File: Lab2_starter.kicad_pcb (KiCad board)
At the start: 4 copper layers, 139.7 x 101.6 mm, 77 parts, among them J1 973582101, J10 Conn_01x02, J11 Conn_01x02, J12 Conn_01x02, J13 Conn_01x02, J14 Conn_01x02, J15 Conn_01x02, J16 Conn_01x02, J2 973582100, J3 973582101, J4 973582100, J5 Conn_01x01, J6 Conn_01x01, J7 Conn_01x02, J8 Conn_01x02, J9 Conn_01x02, Q1 NMOS, Q2 NMOS, SW1 SW_Push_DPDT, U1 IR2010, U2 CT416-HSN820DR, U3 LAUNCHXL-F28P55X_BottomHalf

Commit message: Add Kicad files
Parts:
- C16: moved to B.Cu
- HS1, HS2: footprint ECE462L:HSS-B20-NPR-02 -> ECE462L:HSS-B20-NPS-01
- moved C16 241.9 mm to (50.7, 76.2), turned to -90 degrees
- moved C15 210.3 mm to (72.5, 82.0), turned to -90 degrees
- moved C12 206.2 mm to (76.9, 82.0), turned to -90 degrees
- moved Q1 205.8 mm to (77.5, 78.6)
- moved C9 203.8 mm to (74.7, 82.0), turned to -90 degrees
- moved Q2 197.6 mm to (86.0, 81.8), turned to 180 degrees
- moved HS2 186.2 mm to (80.4, 68.5)
- moved HS1 174.2 mm to (83.9, 92.0), turned to 180 degrees
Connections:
- C1 pad 2: Net-(U2-GND) -> GND
- C12 pad 1: unconnected-(C12-Pad1) -> Vout
- C12 pad 2: unconnected-(C12-Pad2) -> GND
- C15 pad 1: unconnected-(C15-Pad1) -> Vout
- C15 pad 2: unconnected-(C15-Pad2) -> GND
- C16 pad 1: unconnected-(C16-Pad1) -> Vout
- C16 pad 2: unconnected-(C16-Pad2) -> GND
- C3 pad 1: unconnected-(C3-Pad1) -> Vboot
- C3 pad 2: unconnected-(C3-Pad2) -> Vsw
- C4 pad 1: unconnected-(C4-Pad1) -> +12V
- C4 pad 2: unconnected-(C4-Pad2) -> GND
- C6 pad 1: unconnected-(C6-Pad1) -> Vin
- C6 pad 2: unconnected-(C6-Pad2) -> GND
- C9 pad 1: unconnected-(C9-Pad1) -> Vout
- C9 pad 2: unconnected-(C9-Pad2) -> GND
- D2 pad 1: unconnected-(D2-K-Pad1) -> Net-(D2-K)
- D2 pad 2: unconnected-(D2-A-Pad2) -> +12V
- F1 pad 2: unconnected-(F1-Pad2) -> Vin
- J3 pad 1: unconnected-(J3-Pin_1-Pad1) -> Vout
- J6 pad 1: /L_in -> Net-(J6-Pin_1)
- Q1 pad 1: unconnected-(Q1-G-Pad1) -> D'
- Q1 pad 2: unconnected-(Q1-D-Pad2) -> Vout
- Q1 pad 3: unconnected-(Q1-S-Pad3) -> Vsw
- Q2 pad 1: unconnected-(Q2-G-Pad1) -> D
- Q2 pad 2: unconnected-(Q2-D-Pad2) -> Vsw
- Q2 pad 3: unconnected-(Q2-S-Pad3) -> GND
- R13 pad 1: unconnected-(R13-Pad1) -> Net-(D2-K)
- R13 pad 2: unconnected-(R13-Pad2) -> Vboot
- R3 pad 1: unconnected-(R3-Pad1) -> Net-(U1-HO)
- R3 pad 2: unconnected-(R3-Pad2) -> D'
- R4 pad 1: unconnected-(R4-Pad1) -> Net-(U1-LO)
- R4 pad 2: unconnected-(R4-Pad2) -> D
- U1 pad 1: unconnected-(U1-LO-Pad1) -> Net-(U1-LO)
- U1 pad 3: unconnected-(U1-VCC-Pad3) -> +12V
- U1 pad 5: unconnected-(U1-VS-Pad5) -> Vsw
- U1 pad 6: unconnected-(U1-VB-Pad6) -> Vboot
- U1 pad 7: unconnected-(U1-HO-Pad7) -> Net-(U1-HO)
- U1 pad 9: unconnected-(U1-VDD-Pad9) -> +3.3V
- U2 pad 1: unconnected-(U2-IP+-Pad1) -> Vin
- U2 pad 2: unconnected-(U2-IP+-Pad2) -> Vin
- U2 pad 3: unconnected-(U2-IP--Pad3) -> Net-(J6-Pin_1)
- U2 pad 4: unconnected-(U2-IP--Pad4) -> Net-(J6-Pin_1)
- U2 pad 5: Net-(U2-GND) -> GND
- U2 pad 8: unconnected-(U2-VCC-Pad8) -> +3.3V
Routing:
- net Vsw: track 0.00 -> 3.57 mm
- added copper zone on F.Cu, net (none)

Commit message: Moved components around
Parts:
- moved U1 232.0 mm to (47.2, 123.3)
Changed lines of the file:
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@@
 	(footprint "ECE462L:1-2199298-3"
 		(layer "F.Cu")
-		(at 277.34 152.12)
+		(at 47.17 123.31)
 		(tags "1-2199298-3 ")
 		(property "Reference" "U1"

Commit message: Bring over gating loop items
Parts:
- moved C3 151.5 mm to (122.8, 85.9)
- moved C4 151.5 mm to (122.8, 89.0)
- moved C19 151.5 mm to (136.2, 85.9)
- moved D2 151.5 mm to (140.4, 76.3)
- moved R12 142.0 mm to (138.1, 99.8)
- moved R13 142.0 mm to (136.8, 108.0)
- moved R3 142.0 mm to (129.3, 96.9)
- moved R4 142.0 mm to (129.3, 99.8)
- moved U1 58.7 mm to (105.0, 113.3)
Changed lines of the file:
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@@
 	(footprint "Resistor_SMD:R_0805_2012Metric"
 		(layer "F.Cu")
-		(at 271 154.5)
+		(at 136.8075 107.97)
 		(descr "Resistor SMD 0805 (2012 Metric), square (rectangular) end terminal, IPC-7351 nominal, (Body size source: IPC-SM-782 page 72, https://www.pcb-3d.com/wordpress/wp-content/uploads/ipc-sm-782a_amendment_1_and_2.pdf), generated with kicad-footprint-generator")
 		(tags "resistor")
@@
 	(footprint "ECE462L:1-2199298-3"
 		(layer "F.Cu")
-		(at 47.17 123.31)
+		(at 105 113.31)
 		(tags "1-2199298-3 ")
 		(property "Reference" "U1"
@@
 	(footprint "Resistor_SMD:R_0805_2012Metric"
 		(layer "F.Cu")
-		(at 263.505 146.365)
+		(at 129.3125 99.835)
 		(descr "Resistor SMD 0805 (2012 Metric), square (rectangular) end terminal, IPC_7351 nominal, (Body size source: IPC-SM-782 page 72, https://www.pcb-3d.com/wordpress/wp-content/uploads/ipc-sm-782a_amendment_1_and_2.pdf), generated with kicad-footprint-generator")
 		(tags "resistor")
@@
 	(footprint "Diode_SMD:Nexperia_CFP3_SOD-123W"
 		(layer "F.Cu")
-		(at 291.58 65.305)
+		(at 140.4325 76.29)
 		(descr "Nexperia CFP3 (SOD-123W), https://assets.nexperia.com/documents/outline-drawing/SOD123W.pdf")
 		(tags "CFP3 SOD-123W")
@@
 	(footprint "Capacitor_SMD:C_0805_2012Metric"
 		(layer "F.Cu")
-		(at 273.985 77.965)
+		(at 122.8375 88.95)
 		(descr "Capacitor SMD 0805 (2012 Metric), square (rectangular) end terminal, IPC_7351 nominal, (Body size source: IPC-SM-782 page 76, https://www.pcb-3d.com/wordpress/wp-content/uploads/ipc-sm-782a_amendment_1_and_2.pdf, https://docs.google.com/spreadsheets/d/1BsfQQcO9C6DZCsRaXUlFlo91Tg2WpOkGARC1WS5S8t0/edit?usp=sharing), generated with kicad-footprint-generator")
 		(tags "capacitor")
@@
 	(footprint "Resistor_SMD:R_0805_2012Metric"
 		(layer "F.Cu")
-		(at 272.325 146.365)
+		(at 138.1325 99.835)
 		(descr "Resistor SMD 0805 (2012 Metric), square (rectangular) end terminal, IPC_7351 nominal, (Body size source: IPC-SM-782 page 72, https://www.pcb-3d.com/wordpress/wp-content/uploads/ipc-sm-782a_amendment_1_and_2.pdf), generated with kicad-footprint-generator")
 		(tags "resistor")
@@
 	(footprint "Capacitor_SMD:C_0805_2012Metric"
 		(layer "F.Cu")
-		(at 273.985 74.955)
+		(at 122.8375 85.94)
 		(descr "Capacitor SMD 0805 (2012 Metric), square (rectangular) end terminal, IPC_7351 nominal, (Body size source: IPC-SM-782 page 76, https://www.pcb-3d.com/wordpress/wp-content/uploads/ipc-sm-782a_amendment_1_and_2.pdf, https://docs.google.com/spreadsheets/d/1BsfQQcO9C6DZCsRaXUlFlo91Tg2WpOkGARC1WS5S8t0/edit?usp=sharing), generated with kicad-footprint-generator")
 		(tags "capacitor")
@@
 	(footprint "Resistor_SMD:R_0805_2012Metric"
 		(layer "F.Cu")
-		(at 263.505 143.415)
+		(at 129.3125 96.885)
 		(descr "Resistor SMD 0805 (2012 Metric), square (rectangular) end terminal, IPC_7351 nominal, (Body size source: IPC-SM-782 page 72, https://www.pcb-3d.com/wordpress/wp-content/uploads/ipc-sm-782a_amendment_1_and_2.pdf), generated with kicad-footprint-generator")
 		(tags "resistor")
@@
 	(footprint "Capacitor_SMD:C_0805_2012Metric"
 		(layer "F.Cu")
-		(at 287.335 74.955)
+		(at 136.1875 85.94)
 		(descr "Capacitor SMD 0805 (2012 Metric), square (rectangular) end terminal, IPC_7351 nominal, (Body size source: IPC-SM-782 page 76, https://www.pcb-3d.com/wordpress/wp-content/uploads/ipc-sm-782a_amendment_1_and_2.pdf, https://docs.google.com/spreadsheets/d/1BsfQQcO9C6DZCsRaXUlFlo91Tg2WpOkGARC1WS5S8t0/edit?usp=sharing), generated with kicad-footprint-generator")
 		(tags "capacitor")

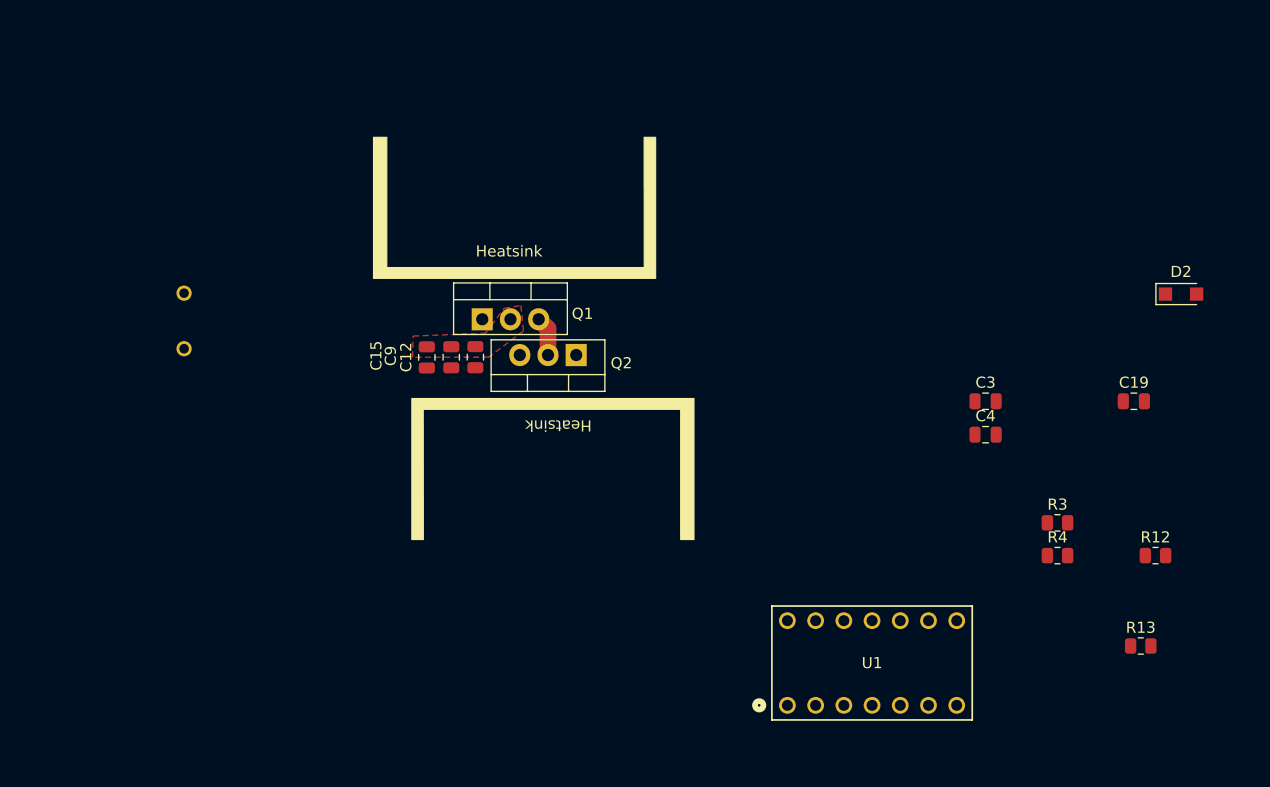
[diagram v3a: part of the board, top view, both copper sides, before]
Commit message: Creating gating loop
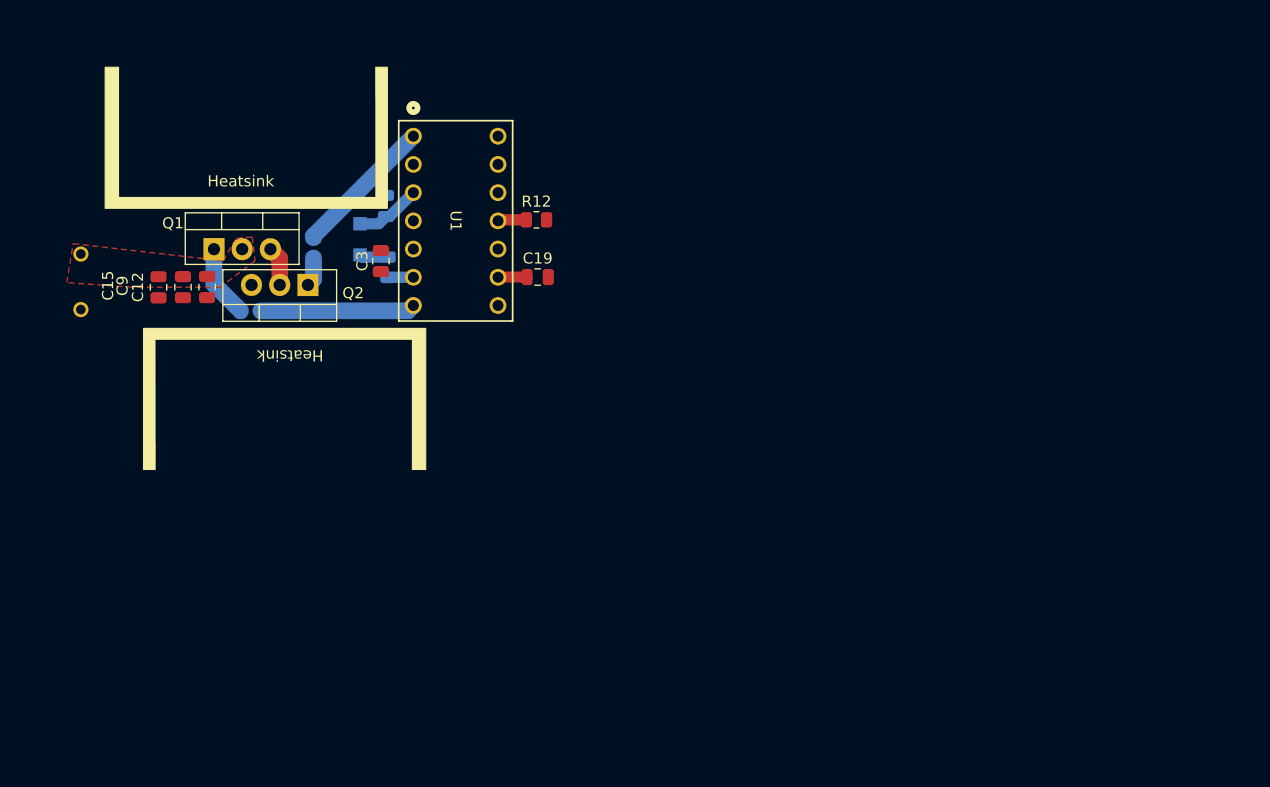
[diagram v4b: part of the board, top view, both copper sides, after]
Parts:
- C4, D2, R13, R3, R4: moved to B.Cu
- moved R13 75.8 mm to (69.0, 73.9), turned to -90 degrees
- moved R3 75.1 mm to (56.7, 77.8), turned to 180 degrees
- moved D2 74.1 mm to (66.5, 71.4), turned to 90 degrees
- moved R4 72.5 mm to (62.3, 72.1), turned to -90 degrees
- moved R12 63.4 mm to (82.4, 69.6)
- moved U1 61.3 mm to (71.3, 62.1), turned to -90 degrees
- moved C4 57.8 mm to (68.9, 68.4), turned to 90 degrees
- moved C3 55.9 mm to (68.4, 73.3), turned to 90 degrees
- moved C19 54.8 mm to (82.5, 74.8)
- moved C15 25.0 mm to (48.4, 75.7)
- moved C12 25.0 mm to (52.8, 75.7)
- moved HS1 25.0 mm to (59.7, 85.7)
- moved HS2 25.0 mm to (56.3, 62.2)
- moved Q1 25.0 mm to (53.4, 72.2)
- moved C9 25.0 mm to (50.6, 75.7)
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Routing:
- net Net-(U1-HO): track 0.00 -> 13.9 mm
- net Net-(U1-LO): track 0.00 -> 12.9 mm
- net D': track 0.00 -> 6.54 mm
- net +12V: track 0.00 -> 5.96 mm
- net D: track 0.00 -> 2.63 mm
- net +3.3V: track 0.00 -> 2.63 mm
- net Net-(D2-K): track 0.00 -> 2.61 mm
- net SD: track 0.00 -> 2.58 mm
- net Vboot: track 0.00 -> 2.29 mm

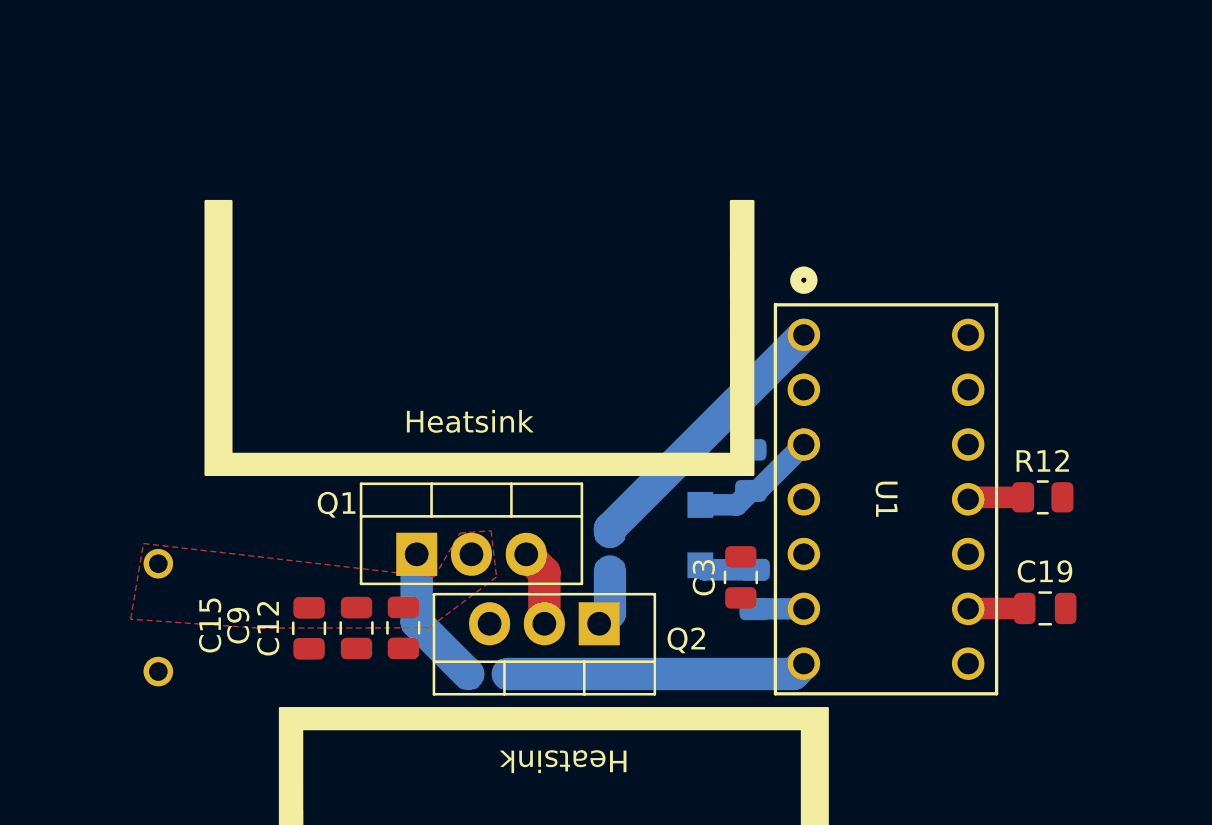
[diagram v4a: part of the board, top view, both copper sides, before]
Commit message: Fixed gating loop
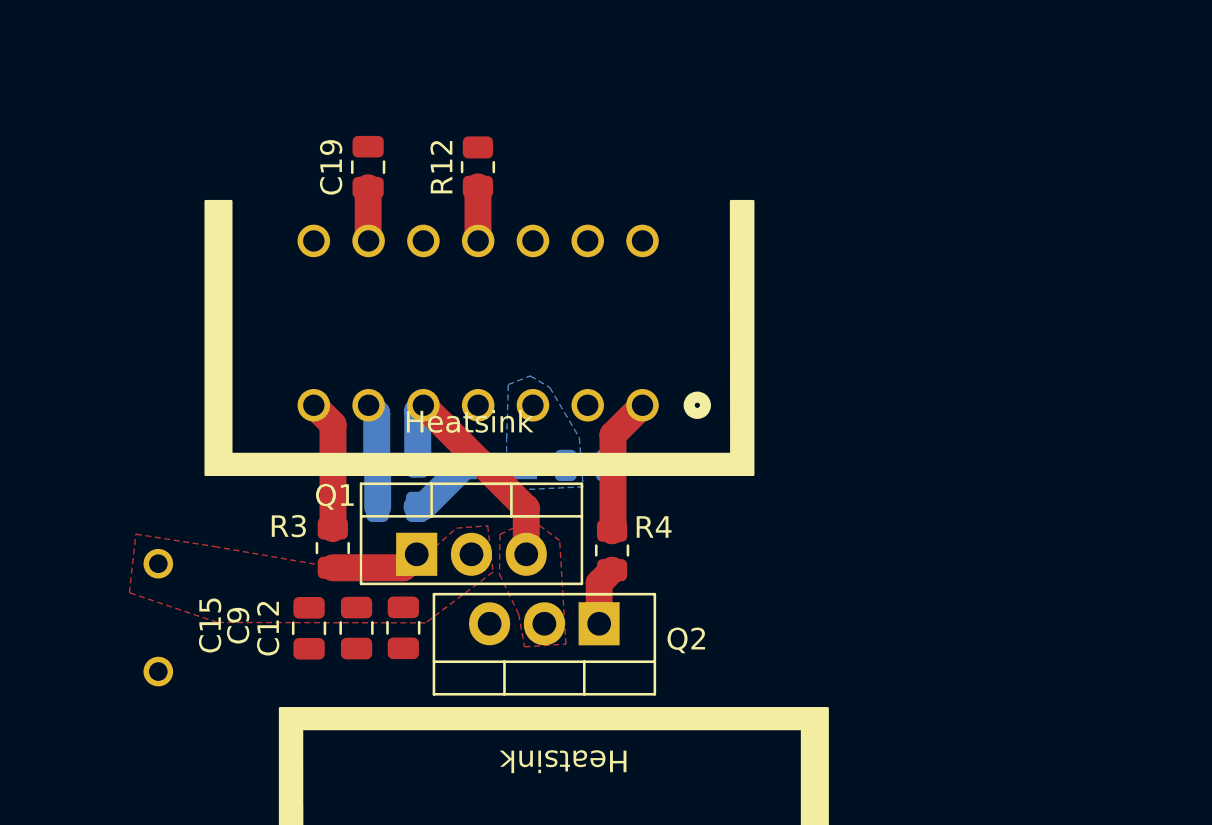
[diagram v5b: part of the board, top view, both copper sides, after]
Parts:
- C3, U1: moved to B.Cu
- R3, R4: moved to F.Cu
- moved C19 37.5 mm to (51.1, 54.3), turned to 90 degrees
- moved R12 30.3 mm to (56.2, 54.3), turned to 90 degrees
- moved R13 17.0 mm to (52.5, 70.0), turned to 180 degrees
- moved C3 16.8 mm to (52.5, 68.0), turned to 0 degrees
- moved D2 10.1 mm to (57.0, 68.2), turned to 0 degrees
- moved R3 9.27 mm to (49.5, 72.0), turned to -90 degrees
- moved U1 8.16 mm to (63.9, 65.3), turned to 180 degrees
- moved C4 7.63 mm to (61.2, 68.1), turned to 0 degrees
- moved R4 0.12 mm to (62.4, 72.1)
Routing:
- net Vsw: track 3.57 -> 11.6 mm
- net Net-(U1-HO): track 13.9 -> 6.08 mm
- net Net-(U1-LO): track 12.9 -> 6.40 mm
- net +12V: track 5.96 -> 0.00 mm
- net Vboot: track 2.29 -> 4.88 mm
- net D': track 6.54 -> 4.15 mm
- added copper zone on B.Cu, net +12V
- added copper zone on F.Cu, net Vsw

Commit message: Everything
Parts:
- C13, C17: moved to B.Cu
- moved H4 271.5 mm to (24.0, 41.5)
- moved C20 266.2 mm to (22.8, 108.0), turned to -90 degrees
- moved C21 263.5 mm to (25.3, 108.1), turned to -90 degrees
- moved J14 256.2 mm to (23.5, 122.8), turned to 180 degrees
- moved H2 255.2 mm to (23.8, 135.8)
- moved J16 252.8 mm to (23.6, 115.7), turned to 180 degrees
- moved C14 249.9 mm to (34.9, 108.8), turned to 180 degrees
- moved TP7 247.7 mm to (28.9, 131.8)
- moved C10 247.6 mm to (33.9, 116.9), turned to 90 degrees
- moved R10 244.6 mm to (49.3, 40.1), turned to 180 degrees
- moved R11 244.4 mm to (49.3, 43.5), turned to 180 degrees
- moved C17 243.3 mm to (46.6, 107.2)
- moved TP11 240.6 mm to (35.0, 131.7)
- moved C7 238.2 mm to (38.5, 116.9), turned to 90 degrees
- moved D3 237.9 mm to (54.8, 40.2)
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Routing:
- net C2000 D : track 0.00 -> 109.8 mm
- net Vsw: track 11.6 -> 80.2 mm
- net Vout: track 0.23 -> 55.2 mm
- net Vout_sens: track 0.00 -> 54.6 mm
- net I_L: track 0.00 -> 54.2 mm
- net C2000 D': track 0.00 -> 47.3 mm
- net D': track 4.15 -> 49.2 mm
- net /ADCINA9: track 0.00 -> 37.1 mm
- net /ADCINA0: track 0.00 -> 30.9 mm
- net Net-(D3-A): track 0.00 -> 18.9 mm
- net Vin_sens: track 0.00 -> 17.8 mm
- net SD: track 2.51 -> 19.4 mm
- net +24V: track 0.00 -> 15.4 mm
- net Net-(D4-A): track 0.00 -> 14.5 mm
- net D: track 2.73 -> 14.8 mm
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- added copper zone on F.Cu, net +24V
- added copper zone on F.Cu, net Vin
- added copper zone on F.Cu, net Vin_sens
- added copper zone on F.Cu, net Vout_sens
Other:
- board size 139.7 x 101.6 mm -> 187.3 x 181.2 mm
